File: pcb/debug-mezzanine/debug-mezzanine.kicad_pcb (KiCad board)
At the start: 2 copper layers, 30.5 x 40.6 mm, 5 parts, among them J1 STM32_SWD, J2 STM32_SWD, J3 PicoTalk, J4 PicoTalk

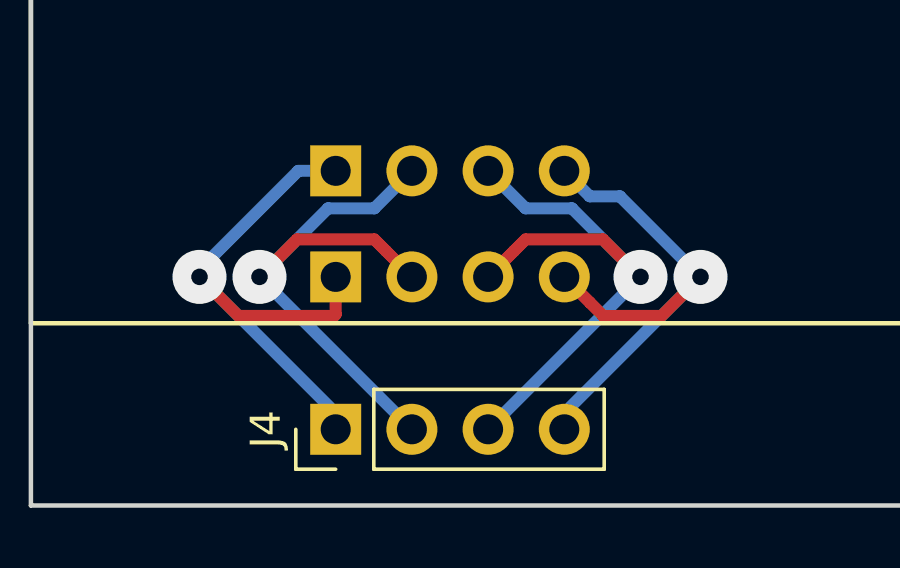
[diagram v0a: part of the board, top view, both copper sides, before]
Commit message: Fixed some pins not being isolated properly on the mezzanine board
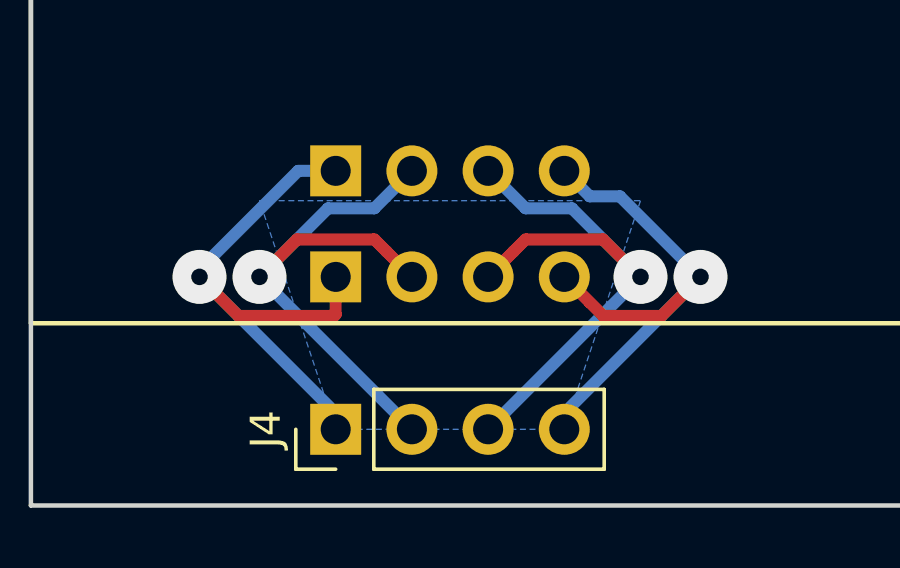
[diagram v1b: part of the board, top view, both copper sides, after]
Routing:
- added copper zone on B.Cu, net (none)
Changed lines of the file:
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@@
     (visible_elements FFFFFF7F)
     (pcbplotparams
-      (layerselection 0x010fc_ffffffff)
+      (layerselection 0x01002_ffffffff)
       (usegerberextensions false)
       (usegerberattributes false)
       (usegerberadvancedattributes false)
-      (creategerberjobfile false)
+      (creategerberjobfile true)
       (excludeedgelayer true)
       (linewidth 0.100000)
@@
       (outputformat 1)
       (mirror false)
-      (drillshape 1)
+      (drillshape 0)
       (scaleselection 1)
-      (outputdirectory ""))
+      (outputdirectory /run/media/teo/C07F-94B3/Treo/mezzanine/))
   )
   (net 0 "")
@@
       )
     )
+  )
+  (zone (net 0) (net_name "") (layer B.Cu) (hatch edge 0.508)
+    (connect_pads (clearance 0.508))
+    (min_thickness 0.254)
+    (fill yes (arc_segments 16) (thermal_gap 0.508) (thermal_bridge_width 0.508))
+    (polygon
+      (pts
+        (xy 134.62 154.94) (xy 132.08 147.32) (xy 144.78 147.32) (xy 142.24 154.94)
+      )
+    )

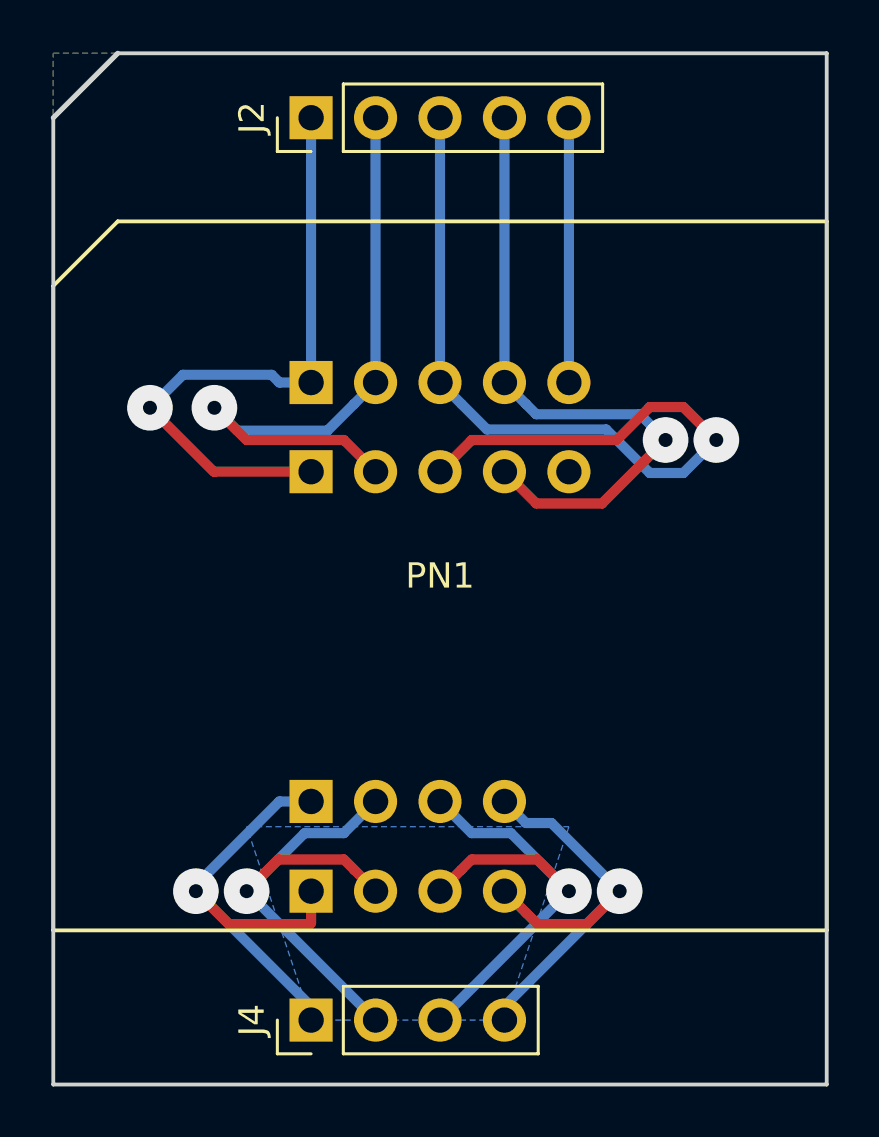
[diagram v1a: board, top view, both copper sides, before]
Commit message: Use the ground plane, Luke!
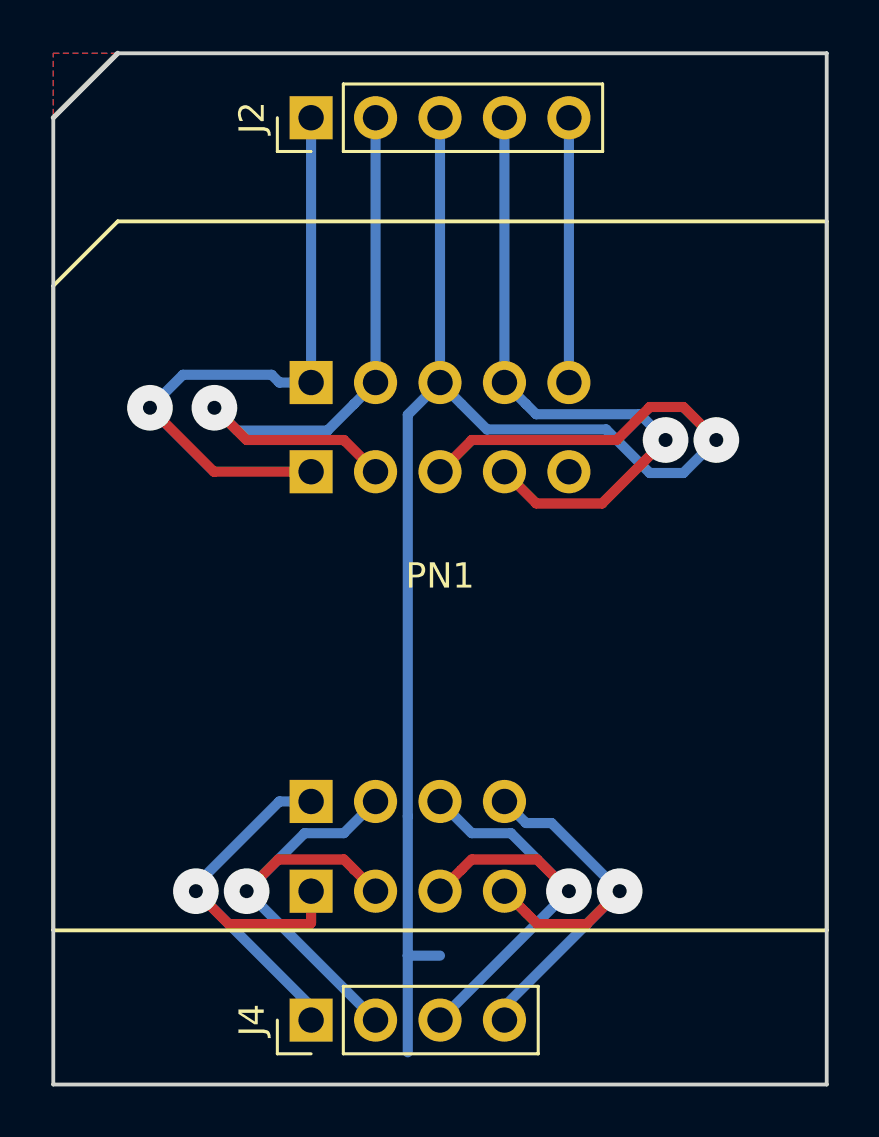
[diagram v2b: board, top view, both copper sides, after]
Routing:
- net GND: track 35.8 -> 64.0 mm
- removed copper zone on B.Cu, net (none)
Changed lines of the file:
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@@
     (thickness 1.6)
     (drawings 6)
-    (tracks 78)
+    (tracks 83)
     (zones 0)
     (modules 5)
@@
   (segment (start 141.550011 131.665012) (end 140.549999 130.665) (width 0.4) (layer B.Cu) (net 2))
   (segment (start 150.590003 132.08) (end 149.290002 133.380001) (width 0.4) (layer B.Cu) (net 2))
+  (segment (start 139.7 129.815001) (end 138.43 131.085001) (width 0.4) (layer B.Cu) (net 2))
+  (segment (start 138.43 131.085001) (end 138.43 146.905003) (width 0.4) (layer B.Cu) (net 2))
+  (segment (start 138.43 152.4) (end 139.7 152.4) (width 0.4) (layer B.Cu) (net 2))
+  (segment (start 138.43 152.4) (end 138.43 156.21) (width 0.4) (layer B.Cu) (net 2))
+  (segment (start 138.43 146.905003) (end 138.43 152.4) (width 0.4) (layer B.Cu) (net 2))
   (segment (start 137.16 129.815001) (end 137.16 119.38) (width 0.4) (layer B.Cu) (net 3))
   (segment (start 132.08 132.08) (end 130.81 130.81) (width 0.4) (layer F.Cu) (net 3))
@@
       )
     )
-  )
-  (zone (net 0) (net_name "") (layer B.Cu) (hatch edge 0.508)
-    (connect_pads (clearance 0.508))
-    (min_thickness 0.254)
-    (fill yes (arc_segments 16) (thermal_gap 0.508) (thermal_bridge_width 0.508))
-    (polygon
-      (pts
-        (xy 134.62 154.94) (xy 132.08 147.32) (xy 144.78 147.32) (xy 142.24 154.94)
-      )
-    )
